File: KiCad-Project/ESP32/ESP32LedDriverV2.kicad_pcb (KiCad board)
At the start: 4 copper layers, 100 x 57 mm, 60 parts, among them J1 Power, J2 LED Terminal, J3 UART, Q10 Q_NMOS_GDS, Q3 Q_NMOS_GDS, Q4 Q_NMOS_GDS, Q5 Q_NMOS_GDS, Q6 Q_NMOS_GDS, Q7 Q_NMOS_GDS, Q8 Q_NMOS_GDS, Q9 Q_NMOS_GDS, SW1 RESET, U1 INA219AxD, U10 TC4420CPA, U11 TC4420CPA, U12 TC4420CPA, U2 R-78C5.0-1.0, U3 AMS1117-3.3, U4 ESP32-WROOM-32, U5 TC4420CPA, U6 TC4420CPA, U7 TC4420CPA, U8 TC4420CPA, U9 TC4420CPA

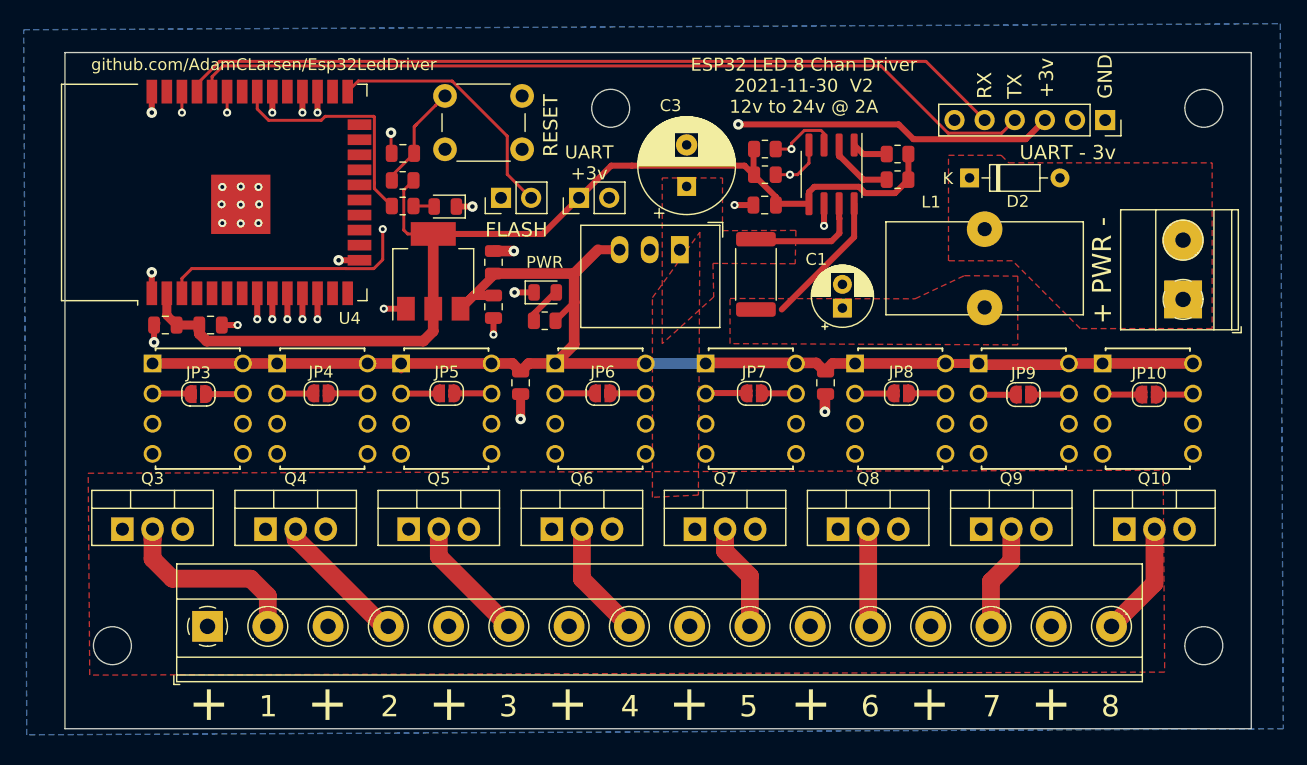
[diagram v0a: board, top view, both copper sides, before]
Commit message: update pin labels
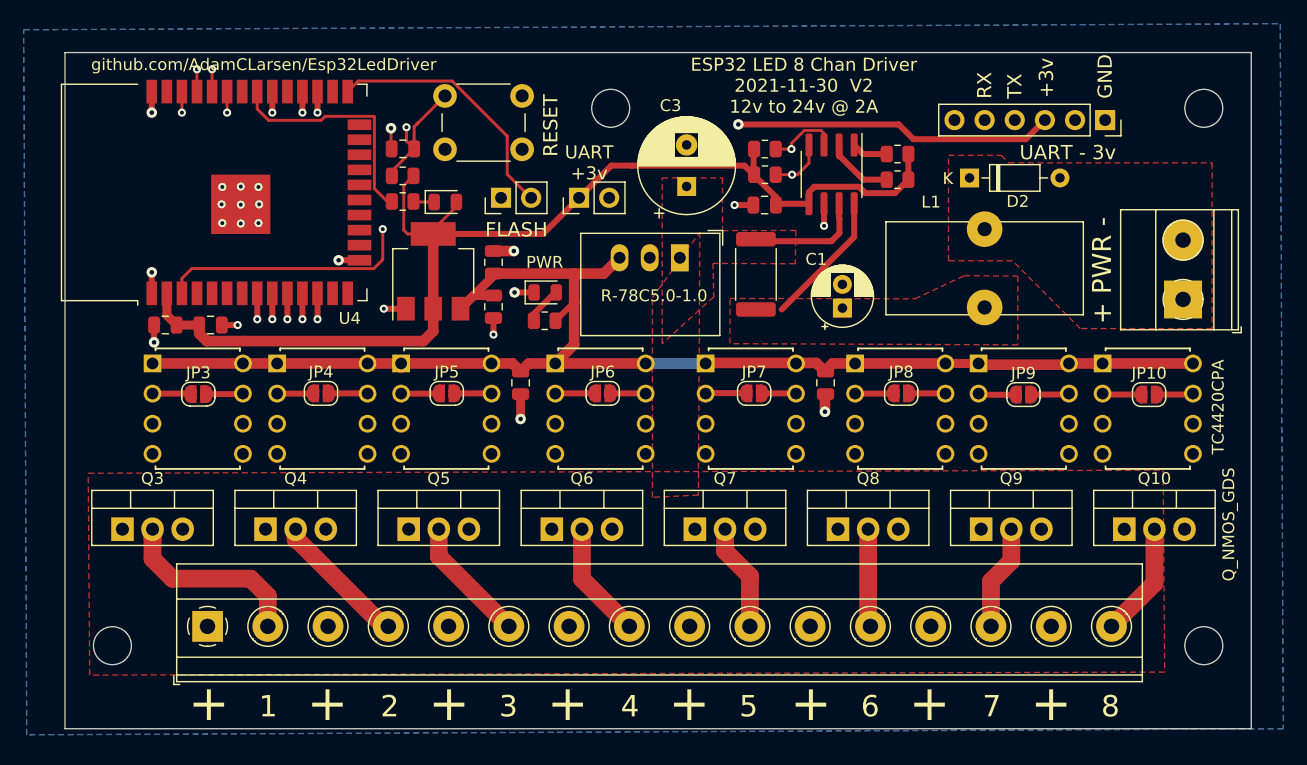
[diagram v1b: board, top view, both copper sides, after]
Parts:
- moved U2 0.68 mm to (95.8, 79.3)
- moved C6 0.38 mm to (72.5, 70.1)
- moved LED2 0.38 mm to (76.1, 74.6), turned to 0 degrees
- moved R10 0.38 mm to (72.5, 74.6)
- moved R9 0.38 mm to (72.5, 72.4)
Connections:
- LED2 pad 1: GND -> Net-(LED2-Pad1)
- LED2 pad 2: Net-(LED2-Pad2) -> +3V3
- R10 pad 2: Net-(LED2-Pad2) -> Net-(LED2-Pad1)
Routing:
- net +3V3: track 92.5 -> 95.7 mm
- net /ESP32/~RESET: track 44.0 -> 41.7 mm, vias 1 -> 2
- net SDA: track 60.0 -> 62.2 mm
- net Net-(LED2-Pad2): track 1.76 -> 0.00 mm
- net Net-(LED2-Pad1): track 0.00 -> 1.76 mm
- net GND: track 46.0 -> 44.7 mm, vias 24 -> 23
- net +5V: track 119.9 -> 118.7 mm
- net /ESP32/UART_RX: track 72.1 -> 71.3 mm, vias 0 -> 1
- net /ESP32/UART_TX: track 69.9 -> 70.0 mm, vias 0 -> 1
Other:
- board text added: "ESP32 Pin layout: LED - ~IO19 SDA - IO21 SCL - IO22 INA219 - ADR 45"
- board text removed: "ESP32 Pin layout: LED - IO19 SDA - IO21 SCL - IO22"

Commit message: Reset annotations
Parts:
- Q1: renamed from Q3; value Q_NMOS_GDS -> P30N06LE
- Q2: renamed from Q4; value Q_NMOS_GDS -> P30N06LE
- Q3: renamed from Q5; value Q_NMOS_GDS -> P30N06LE
- Q4: renamed from Q6; value Q_NMOS_GDS -> P30N06LE
- Q5: renamed from Q7; value Q_NMOS_GDS -> P30N06LE
- Q6: renamed from Q8; value Q_NMOS_GDS -> P30N06LE
- Q7: renamed from Q9; value Q_NMOS_GDS -> P30N06LE
- Q8: renamed from Q10; value Q_NMOS_GDS -> P30N06LE
- moved JP10 2.45 mm to (89.8, 74.2), turned to 270 degrees
- renumbered C3 to C1, C9 to C10, C1 to C3, C10 to C8, C8 to C9, D2 to D1, JP3 to JP1, JP2 to JP10, JP4 to JP2, JP5 to JP3, JP6 to JP4, JP7 to JP5, JP8 to JP6, JP9 to JP7, JP10 to JP8, JP1 to JP9, R3 to R1, R4 to R2, R5 to R3, R6 to R4, R7 to R5, R8 to R6, R9 to R7, R10 to R8, U2 to U1, U12 to U10, U3 to U11, U4 to U12, U1 to U2, U5 to U3, U6 to U4, U7 to U5, U8 to U6, U9 to U7, U10 to U8, U11 to U9
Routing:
- net SCL: track 66.2 -> 61.2 mm
- net SDA: track 62.2 -> 58.2 mm
- net /ESP32/UART_VCC: track 40.5 -> 43.1 mm, vias 1 -> 0
